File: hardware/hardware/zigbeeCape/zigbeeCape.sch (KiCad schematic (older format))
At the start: 46 parts, among them J1 Conn_ARM_JTAG_SWD_10, SW1 SW_MEC_5E, SW2 SW_MEC_5E, SW3 SW_MEC_5E, SW4 SW_MEC_5E, SW5 SW_MEC_5E, U1 CC1352R, Y1 32.768kHz, Y2 48MHz

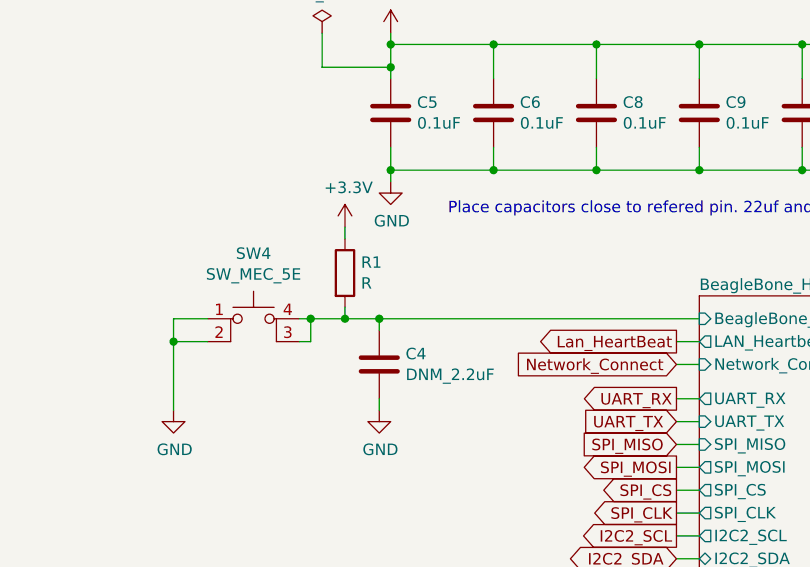
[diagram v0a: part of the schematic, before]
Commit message: Updated R1 on schematic, Updated R1 on BOM, add alt for button
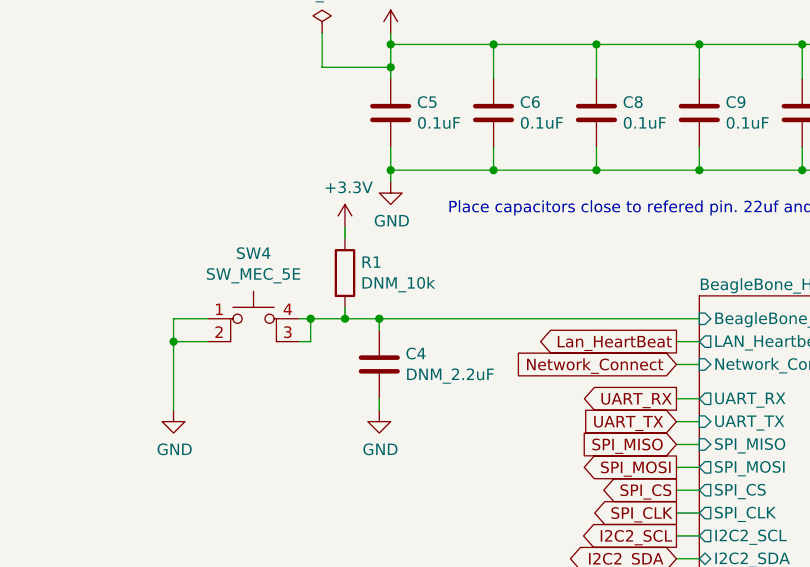
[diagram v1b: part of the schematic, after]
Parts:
- R1: value R -> DNM_10k
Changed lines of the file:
@@
 P 2450 3650
 F 0 "R1" H 2520 3696 50  0000 L CNN
-F 1 "R" H 2520 3605 50  0000 L CNN
+F 1 "DNM_10k" H 2520 3605 50  0000 L CNN
 F 2 "Resistor_SMD:R_0603_1608Metric_Pad0.98x0.95mm_HandSolder" V 2380 3650 50  0001 C CNN
 F 3 "~" H 2450 3650 50  0001 C CNN

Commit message: Changed push button, Started layout
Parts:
- SW1, SW2, SW3, SW4, SW5: footprint Button_Switch_THT:SW_PUSH_6mm -> zigbeeCape:SMD_PUSH_BUTTON
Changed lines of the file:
@@
 F 0 "SW1" H 1100 6185 50  0000 C CNN
 F 1 "SW_MEC_5E" H 1100 6094 50  0000 C CNN
-F 2 "Button_Switch_THT:SW_PUSH_6mm" H 1100 6100 50  0001 C CNN
+F 2 "zigbeeCape:SMD_PUSH_BUTTON" H 1100 6100 50  0001 C CNN
 F 3 "http://www.apem.com/int/index.php?controller=attachment&id_attachment=1371" H 1100 6100 50  0001 C CNN
 	1    1100 5800
@@
 F 0 "SW2" H 1100 6885 50  0000 C CNN
 F 1 "SW_MEC_5E" H 1100 6794 50  0000 C CNN
-F 2 "Button_Switch_THT:SW_PUSH_6mm" H 1100 6800 50  0001 C CNN
+F 2 "zigbeeCape:SMD_PUSH_BUTTON" H 1100 6800 50  0001 C CNN
 F 3 "http://www.apem.com/int/index.php?controller=attachment&id_attachment=1371" H 1100 6800 50  0001 C CNN
 	1    1100 6500
@@
 F 0 "SW3" H 1100 7585 50  0000 C CNN
 F 1 "SW_MEC_5E" H 1100 7494 50  0000 C CNN
-F 2 "Button_Switch_THT:SW_PUSH_6mm" H 1100 7500 50  0001 C CNN
+F 2 "zigbeeCape:SMD_PUSH_BUTTON" H 1100 7500 50  0001 C CNN
 F 3 "http://www.apem.com/int/index.php?controller=attachment&id_attachment=1371" H 1100 7500 50  0001 C CNN
 	1    1100 7200
@@
 F 0 "SW5" H 4150 1285 50  0000 C CNN
 F 1 "SW_MEC_5E" H 4150 1194 50  0000 C CNN
-F 2 "Button_Switch_THT:SW_PUSH_6mm" H 4150 1200 50  0001 C CNN
+F 2 "zigbeeCape:SMD_PUSH_BUTTON" H 4150 1200 50  0001 C CNN
 F 3 "http://www.apem.com/int/index.php?controller=attachment&id_attachment=1371" H 4150 1200 50  0001 C CNN
 	1    4150 900
@@
 F 0 "SW4" H 2050 4335 50  0000 C CNN
 F 1 "SW_MEC_5E" H 2050 4244 50  0000 C CNN
-F 2 "Button_Switch_THT:SW_PUSH_6mm" H 2050 4250 50  0001 C CNN
+F 2 "zigbeeCape:SMD_PUSH_BUTTON" H 2050 4250 50  0001 C CNN
 F 3 "http://www.apem.com/int/index.php?controller=attachment&id_attachment=1371" H 2050 4250 50  0001 C CNN
 	1    2050 3950
@@
 Text GLabel 3900 4300 0    50   Input ~ 0
 UART_TX
-Text GLabel 3900 4400 0    50   Input ~ 0
-SPI_MISO
 Text GLabel 3900 4500 0    50   Output ~ 0
 SPI_MOSI
@@
 Text Notes 8200 3100 0    39   ~ 0
 This symbol looks gross.\nMight endup changing it.
+Text GLabel 3900 4400 0    50   Input ~ 0
+SPI_MISO
 $EndSCHEMATC

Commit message: Layout Planning done, uC Done
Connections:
- net BeagleBone_Headers/BeagleBone_Reset: no longer C4.1, R1.2, SW4.3 (K), SW4.4 (A)
- new net: C4.1, R1.2, SW4.3 (K), SW4.4 (A)
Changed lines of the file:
@@
 F0 "BeagleBone_Headers" 50
 F1 "BeagleBone_Headers.sch" 50
-F2 "BeagleBone_Reset" I L 4000 3850 50
+F2 "BeagleBone_Reset" I R 4800 3850 50
 F3 "LAN_Heartbeat" O L 4000 3950 50
 F4 "SPI_MISO" I L 4000 4400 50

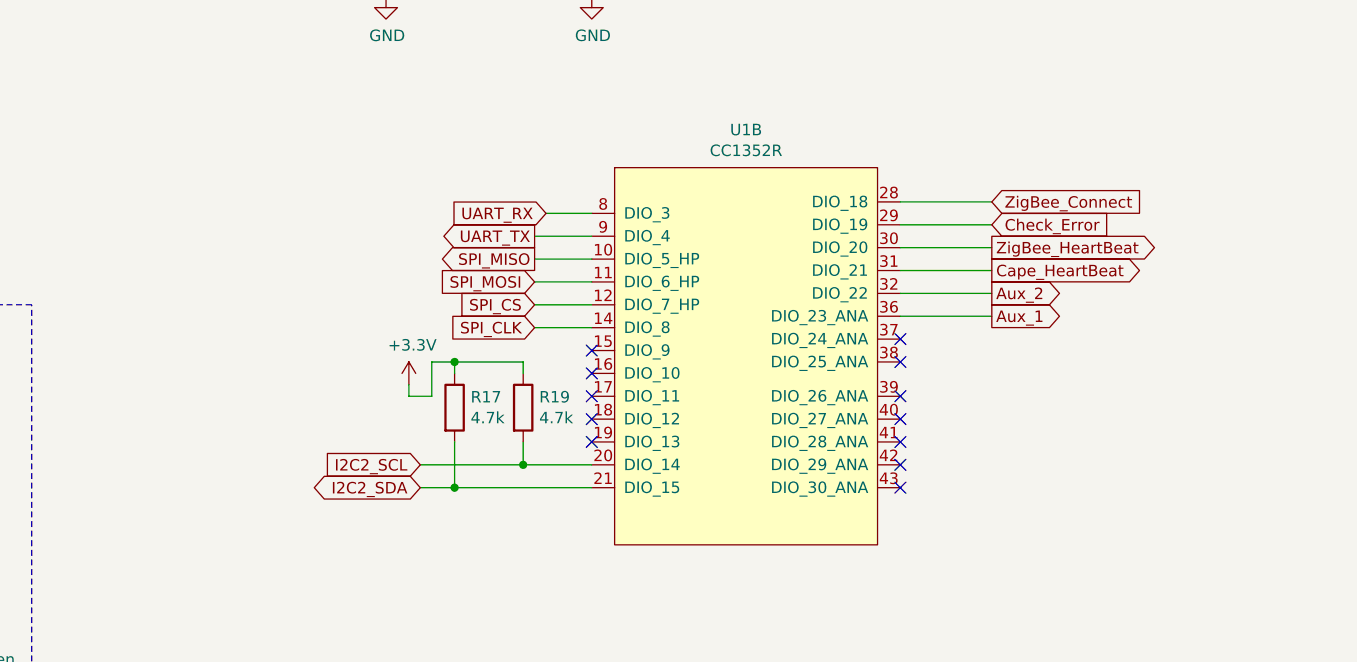
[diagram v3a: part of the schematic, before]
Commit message: Buttons, most LEDs are done
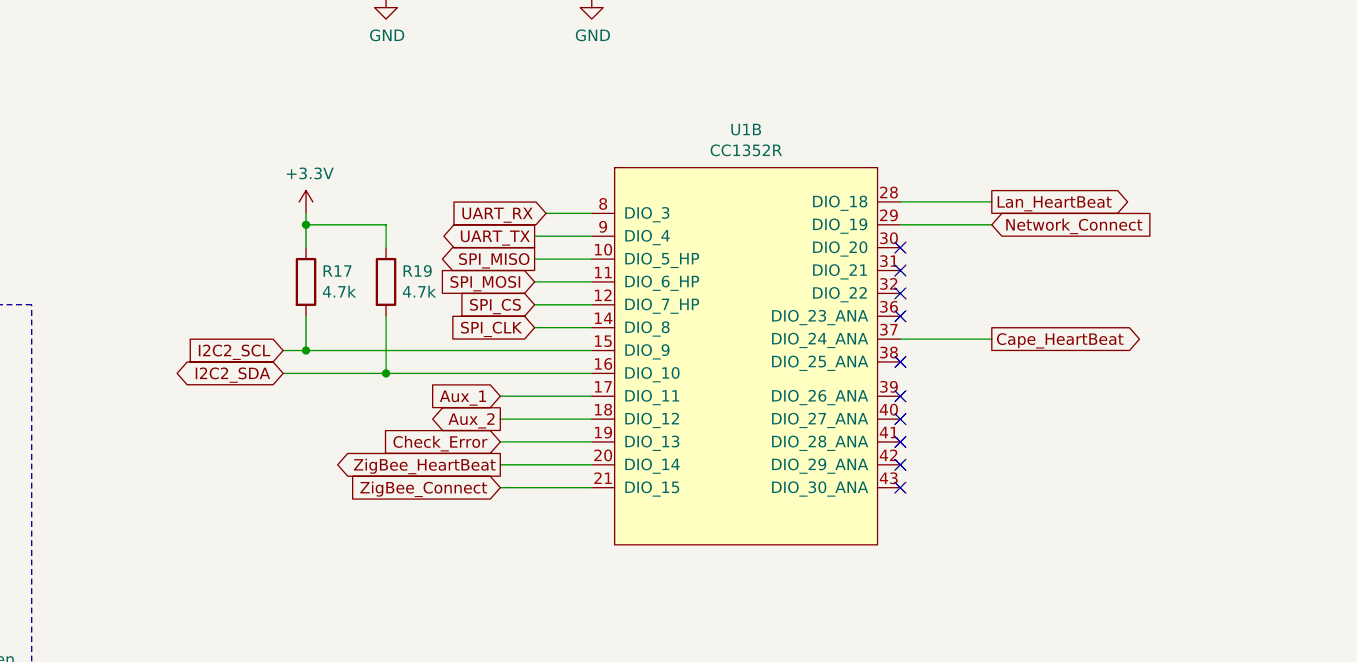
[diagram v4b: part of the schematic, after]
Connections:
- net Aux_1: now also U1.17 (DIO_11); no longer U1.36 (DIO_23_ANA)
- net Aux_2: now also U1.18 (DIO_12); no longer U1.32 (DIO_22)
- net Cape_HeartBeat: now also U1.37 (DIO_24_ANA); no longer U1.31 (DIO_21)
- net Check_Error: now also U1.19 (DIO_13); no longer U1.29 (DIO_19)
- net I2C2_SCL: now also R17.2, U1.15 (DIO_9); no longer R19.2, U1.20 (DIO_14)
- net I2C2_SDA: now also R19.2, U1.16 (DIO_10); no longer R17.2, U1.21 (DIO_15)
- net Lan_HeartBeat: now also U1.28 (DIO_18)
- net Network_Connect: now also U1.29 (DIO_19)
- net ZigBee_Connect: now also U1.21 (DIO_15); no longer U1.28 (DIO_18)
- net ZigBee_HeartBeat: now also U1.20 (DIO_14); no longer U1.30 (DIO_20)
- no-connect marks 12 -> 10
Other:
- moved on the sheet: R17, R19
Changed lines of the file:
@@
 L Device:R R19
 U 1 1 608B8299
-P 7550 5750
-F 0 "R19" H 7620 5796 50  0000 L CNN
-F 1 "4.7k" H 7620 5705 50  0000 L CNN
-F 2 "Resistor_SMD:R_0603_1608Metric_Pad0.98x0.95mm_HandSolder" V 7480 5750 50  0001 C CNN
-F 3 "~" H 7550 5750 50  0001 C CNN
-	1    7550 5750
+P 6950 5200
+F 0 "R19" H 7020 5246 50  0000 L CNN
+F 1 "4.7k" H 7020 5155 50  0000 L CNN
+F 2 "Resistor_SMD:R_0603_1608Metric_Pad0.98x0.95mm_HandSolder" V 6880 5200 50  0001 C CNN
+F 3 "~" H 6950 5200 50  0001 C CNN
+	1    6950 5200
 	1    0    0    -1
 $EndComp
@@
 L Device:R R17
 U 1 1 608B8AB3
-P 7250 5750
-F 0 "R17" H 7320 5796 50  0000 L CNN
-F 1 "4.7k" H 7320 5705 50  0000 L CNN
-F 2 "Resistor_SMD:R_0603_1608Metric_Pad0.98x0.95mm_HandSolder" V 7180 5750 50  0001 C CNN
-F 3 "~" H 7250 5750 50  0001 C CNN
-	1    7250 5750
+P 6600 5200
+F 0 "R17" H 6670 5246 50  0000 L CNN
+F 1 "4.7k" H 6670 5155 50  0000 L CNN
+F 2 "Resistor_SMD:R_0603_1608Metric_Pad0.98x0.95mm_HandSolder" V 6530 5200 50  0001 C CNN
+F 3 "~" H 6600 5200 50  0001 C CNN
+	1    6600 5200
 	1    0    0    -1
 $EndComp
@@
 L power:+3.3V #PWR028
 U 1 1 608BA24C
-P 7050 5650
-F 0 "#PWR028" H 7050 5500 50  0001 C CNN
-F 1 "+3.3V" H 7065 5823 50  0000 C CNN
-F 2 "" H 7050 5650 50  0001 C CNN
-F 3 "" H 7050 5650 50  0001 C CNN
-	1    7050 5650
-	1    0    0    -1
-$EndComp
-Wire Wire Line
-	7550 5600 7550 5550
-Wire Wire Line
-	7550 5550 7250 5550
-Wire Wire Line
-	7250 5550 7250 5600
-Wire Wire Line
-	7250 5550 7150 5550
-Wire Wire Line
-	7150 5550 7150 5700
-Wire Wire Line
-	7150 5700 7050 5700
-Wire Wire Line
-	7050 5700 7050 5650
-Connection ~ 7250 5550
-Wire Wire Line
-	7850 6000 7550 6000
-Wire Wire Line
-	7550 6000 7550 5900
-Wire Wire Line
-	7850 6100 7250 6100
-Wire Wire Line
-	7250 6100 7250 5900
-Text GLabel 7100 6000 0    50   Input ~ 0
+P 6600 4900
+F 0 "#PWR028" H 6600 4750 50  0001 C CNN
+F 1 "+3.3V" H 6615 5073 50  0000 C CNN
+F 2 "" H 6600 4900 50  0001 C CNN
+F 3 "" H 6600 4900 50  0001 C CNN
+	1    6600 4900
+	1    0    0    -1
+$EndComp
+Text GLabel 6500 5500 0    50   Input ~ 0
 I2C2_SCL
-Text GLabel 7100 6100 0    50   BiDi ~ 0
+Text GLabel 6500 5600 0    50   BiDi ~ 0
 I2C2_SDA
-Wire Wire Line
-	7550 6000 7100 6000
-Connection ~ 7550 6000
-Wire Wire Line
-	7250 6100 7100 6100
-Connection ~ 7250 6100
 $Comp
 L power:GND #PWR014
@@
 	4900 900  4900 1000
 Connection ~ 4900 900
-Text GLabel 9600 4850 2    50   Input ~ 0
-ZigBee_Connect
-Text GLabel 9600 4950 2    50   Input ~ 0
-Check_Error
-Text GLabel 9600 5050 2    50   Output ~ 0
-ZigBee_HeartBeat
-Text GLabel 9600 5150 2    50   Output ~ 0
+Text GLabel 9600 5450 2    50   Output ~ 0
 Cape_HeartBeat
-Text GLabel 9600 5250 2    50   Output ~ 0
-Aux_2
-Text GLabel 9600 5350 2    50   Output ~ 0
-Aux_1
-Wire Wire Line
-	9600 5350 9200 5350
-Wire Wire Line
-	9600 5250 9200 5250
-Wire Wire Line
-	9600 5150 9200 5150
-Wire Wire Line
-	9600 5050 9200 5050
-Wire Wire Line
-	9600 4950 9200 4950
-Wire Wire Line
-	9600 4850 9200 4850
 $Comp
 L power:+3.3V #PWR010
@@
 	1    0    0    -1
 $EndComp
-NoConn ~ 9200 5450
 NoConn ~ 9200 5550
 NoConn ~ 9200 5700
@@
 NoConn ~ 9200 6000
 NoConn ~ 9200 6100
-NoConn ~ 7850 5500
-NoConn ~ 7850 5600
-NoConn ~ 7850 5700
-NoConn ~ 7850 5800
-NoConn ~ 7850 5900
 $Comp
 L power:PWR_FLAG #FLG0101
@@
 Text GLabel 3900 4400 0    50   Input ~ 0
 SPI_MISO
+Text GLabel 9600 4950 2    50   Input ~ 0
+Network_Connect
+Text GLabel 9600 4850 2    50   Output ~ 0
+Lan_HeartBeat
+Text GLabel 7450 6100 0    50   Input ~ 0
+ZigBee_Connect
+Text GLabel 7450 6000 0    50   Output ~ 0
+ZigBee_HeartBeat
+Text GLabel 7450 5700 0    50   Input ~ 0
+Aux_1
+Text GLabel 7450 5800 0    50   Output ~ 0
+Aux_2
+Text GLabel 7450 5900 0    50   Input ~ 0
+Check_Error
+Wire Wire Line
+	7850 5900 7450 5900
+Wire Wire Line
+	7450 5800 7850 5800
+Wire Wire Line
+	7850 5700 7450 5700
+Wire Wire Line
+	7850 5600 6950 5600
+Wire Wire Line
+	6500 5500 6600 5500
+Wire Wire Line
+	6950 5350 6950 5600
+Connection ~ 6950 5600
+Wire Wire Line
+	6950 5600 6500 5600
+Wire Wire Line
+	6600 5500 6600 5350
+Connection ~ 6600 5500
+Wire Wire Line
+	6600 5500 7850 5500
+Wire Wire Line
+	6950 5050 6950 4950
+Wire Wire Line
+	6950 4950 6600 4950
+Wire Wire Line
+	6600 4950 6600 4900
+Wire Wire Line
+	6600 5050 6600 4950
+Connection ~ 6600 4950
+Wire Wire Line
+	9200 4850 9600 4850
+Wire Wire Line
+	9600 4950 9200 4950
+Wire Wire Line
+	9200 5450 9600 5450
+NoConn ~ 9200 5050
+NoConn ~ 9200 5150
+NoConn ~ 9200 5250
+NoConn ~ 9200 5350
+Wire Wire Line
+	7450 6000 7850 6000
+Wire Wire Line
+	7850 6100 7450 6100
 $EndSCHEMATC
